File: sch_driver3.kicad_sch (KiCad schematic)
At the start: 17 parts, among them Q3 PSMN4R0-30YLDX, U13 TS5A3159ADCK, U2 ADA4099-2xR, U23 OPA333

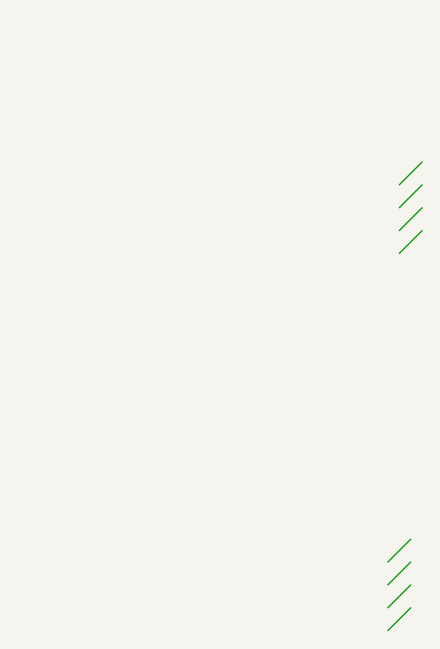
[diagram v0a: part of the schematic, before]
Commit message: Finished schematic refactor to six A-sheets. Updated PCB.
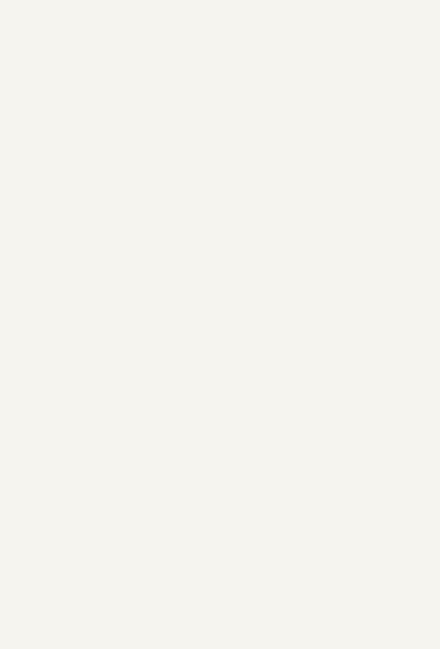
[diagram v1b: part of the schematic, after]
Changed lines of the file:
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@@
 	(title_block
 		(title "PBM Driver 4 V2")
-		(date "23-DEC-2025")
+		(date "24-DEC-2025")
 		(rev "A")
 		(comment 1 "Part Number: PCB104 Rev A")
@@
 		(color 0 0 0 0)
 	)
-	(bus_entry
-		(at 389.89 226.06)
-		(size -2.54 2.54)
-		(stroke
-			(width 0)
-			(type default)
-		)
-	)
-	(bus_entry
-		(at 389.89 223.52)
-		(size -2.54 2.54)
-		(stroke
-			(width 0)
-			(type default)
-		)
-	)
-	(bus_entry
-		(at 391.16 181.61)
-		(size -2.54 2.54)
-		(stroke
-			(width 0)
-			(type default)
-		)
-	)
-	(bus_entry
-		(at 391.16 179.07)
-		(size -2.54 2.54)
-		(stroke
-			(width 0)
-			(type default)
-		)
-	)
-	(bus_entry
-		(at 389.89 220.98)
-		(size -2.54 2.54)
-		(stroke
-			(width 0)
-			(type default)
-		)
-	)
-	(bus_entry
-		(at 391.16 184.15)
-		(size -2.54 2.54)
-		(stroke
-			(width 0)
-			(type default)
-		)
-	)
-	(bus_entry
-		(at 391.16 176.53)
-		(size -2.54 2.54)
-		(stroke
-			(width 0)
-			(type default)
-		)
-	)
-	(bus_entry
-		(at 389.89 218.44)
-		(size -2.54 2.54)
-		(stroke
-			(width 0)
-			(type default)
-		)
-	)
 	(wire

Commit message: Routing WIP. Prep to look at SOT-23 op amps for U1 and U2. Added convenience link to Git Bash.
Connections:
- net OUT: now reaches C33.2, R13.1, U2.1
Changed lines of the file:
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@@
+		)
+	)
+	(label "OUT"
+		(at 110.49 53.34 0)
+		(effects
+			(font
+				(size 1.27 1.27)
+			)
+			(justify left bottom)
 		)
 	)

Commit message: Routing WIP with SOT-23 op amps
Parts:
- added C53: 100pF, $Local:C_0603_1608Metric, symbol $Local:C
- added U5: ADA4099-2xR, Package_TO_SOT_SMD:TSOT-23-6, symbol Amplifier_Operational:ADA4099-1xUJ
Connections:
- net +12V: now also U5.6 (V+)
- net DAC: now also C53.1
- net FB: now also U5.4 (-)
- net GND: now also C53.2, U5.2 (V-), U5.5 (~{SHDN})
- net OUT: now also U5.1
- net REF: now also U5.3 (+)

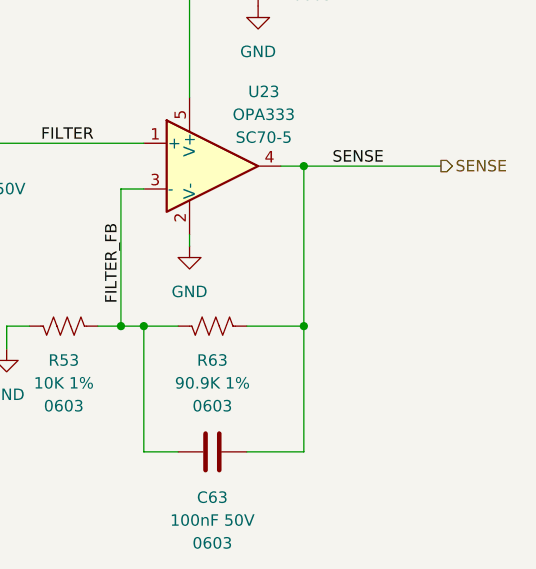
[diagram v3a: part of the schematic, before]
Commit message: Added pull-downs to output of Sense filter op amps
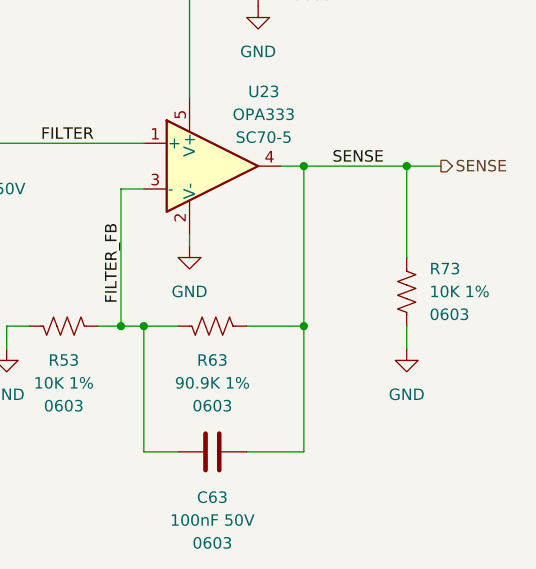
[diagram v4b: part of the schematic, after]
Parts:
- added R73: 10K 1%, $Local:R_0603_1608Metric, symbol $Local:R_0603_10K
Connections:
- net GND: now also R73.2
- net SENSE: now also R73.1
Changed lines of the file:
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@@
 		(color 0 0 0 0)
 	)
+	(junction
+		(at 237.49 71.12)
+		(diameter 0)
+		(color 0 0 0 0)
+	)
 	(wire
 		(pts
@@
 	(wire
 		(pts
+			(xy 237.49 71.12) (xy 241.3 71.12)
+		)
+		(stroke
+			(width 0)
+			(type default)
+		)
+	)
+	(wire
+		(pts
 			(xy 208.28 88.9) (xy 212.09 88.9)
 		)
@@
 	(wire
 		(pts
+			(xy 237.49 71.12) (xy 237.49 81.28)
+		)
+		(stroke
+			(width 0)
+			(type default)
+		)
+	)
+	(wire
+		(pts
 			(xy 54.61 55.88) (xy 54.61 53.34)
 		)
@@
 	(wire
 		(pts
-			(xy 226.06 71.12) (xy 241.3 71.12)
+			(xy 226.06 71.12) (xy 237.49 71.12)
 		)
 		(stroke
@@
 		(pts
 			(xy 147.32 58.42) (xy 147.32 60.96)
+		)
+		(stroke
+			(width 0)
+			(type default)
+		)
+	)
+	(wire
+		(pts
+			(xy 237.49 88.9) (xy 237.49 91.44)
 		)
 		(stroke
@@
 					(unit 1)
 				)
+			)
+		)
+	)
+	(symbol
+		(lib_id "$Local:R_0603_10K")
+		(at 237.49 85.09 0)
+		(unit 1)
+		(exclude_from_sim no)
+		(in_bom yes)
+		(on_board yes)
+		(dnp no)
+		(fields_autoplaced yes)
+		(property "Reference" "R73"
+			(at 240.03 82.5499 0)
+			(effects
+				(font
+					(size 1.27 1.27)
+				)
+				(justify left)
+			)
+		)
+		(property "Value" "10K 1%"
+			(at 240.03 85.0899 0)
+			(effects
+				(font
+					(size 1.27 1.27)
+				)
+				(justify left)
+			)
+		)
+		(property "Footprint" "$Local:R_0603_1608Metric"
+			(at 238.506 85.344 90)
+			(effects
+				(font
+					(size 1.27 1.27)
+				)
+				(hide yes)
+			)
+		)
+		(property "Datasheet" "~"
+			(at 237.49 85.09 0)
+			(effects
+				(font
+					(size 1.27 1.27)
+				)
+				(hide yes)
+			)
+		)
+		(property "Description" "RES SMD 10K OHM 1% 1/10W 0603"
+			(at 237.49 85.09 0)
+			(effects
+				(font
+					(size 1.27 1.27)
+				)
+				(hide yes)
+			)
+		)
+		(property "Size" "0603"
+			(at 240.03 87.6299 0)
+			(effects
+				(font
+					(size 1.27 1.27)
+				)
+				(justify left)
+			)
+		)
+		(property "PN" ""
+			(at 237.49 85.09 0)
+			(effects
+				(font
+					(size 1.27 1.27)
+				)
+				(hide yes)
+			)
+		)
+		(pin "1"
+		)
+		(pin "2"
+		)
+		(instances
+			(project "pbm_driver4_v2"
+				(path "/04797749-7aaf-42f7-a5f4-0b9aeb0ad7be/8ef61302-d9b8-4eae-8136-04cfb82addb3"
+					(reference "R73")
+					(unit 1)
+				)
+			)
+		)
+	)
+	(symbol
+		(lib_id "$Local:GND")
+		(at 237.49 91.44 0)
+		(unit 1)
+		(exclude_from_sim no)
+		(in_bom yes)
+		(on_board yes)
+		(dnp no)
+		(fields_autoplaced yes)
+		(property "Reference" "#PWR036"
+			(at 237.49 97.79 0)
+			(effects
+				(font
+					(size 1.27 1.27)
+				)
+				(hide yes)
+			)
+		)
+		(property "Value" "GND"
+			(at 237.49 96.52 0)
+			(effects
+				(font
+					(size 1.27 1.27)
+				)
+			)
+		)
+		(property "Footprint" ""
+			(at 237.49 91.44 0)
+			(effects
+				(font
+					(size 1.27 1.27)
+				)
+				(hide yes)
+			)
+		)
+		(property "Datasheet" ""
+			(at 237.49 91.44 0)
+			(effects
+				(font
+					(size 1.27 1.27)
+				)
+				(hide yes)
+			)
+		)
+		(property "Description" "Power symbol creates a global label with name \"GND\" , ground"
+			(at 237.49 91.44 0)
+			(effects
+				(font
+					(size 1.27 1.27)
+				)
+				(hide yes)
+			)
+		)
+		(pin "1"
+		)
+		(instances
+			(project "pbm_driver4_v2"
+				(path "/04797749-7aaf-42f7-a5f4-0b9aeb0ad7be/8ef61302-d9b8-4eae-8136-04cfb82addb3"
+					(reference "#PWR036")
+					(unit 1)
+				)

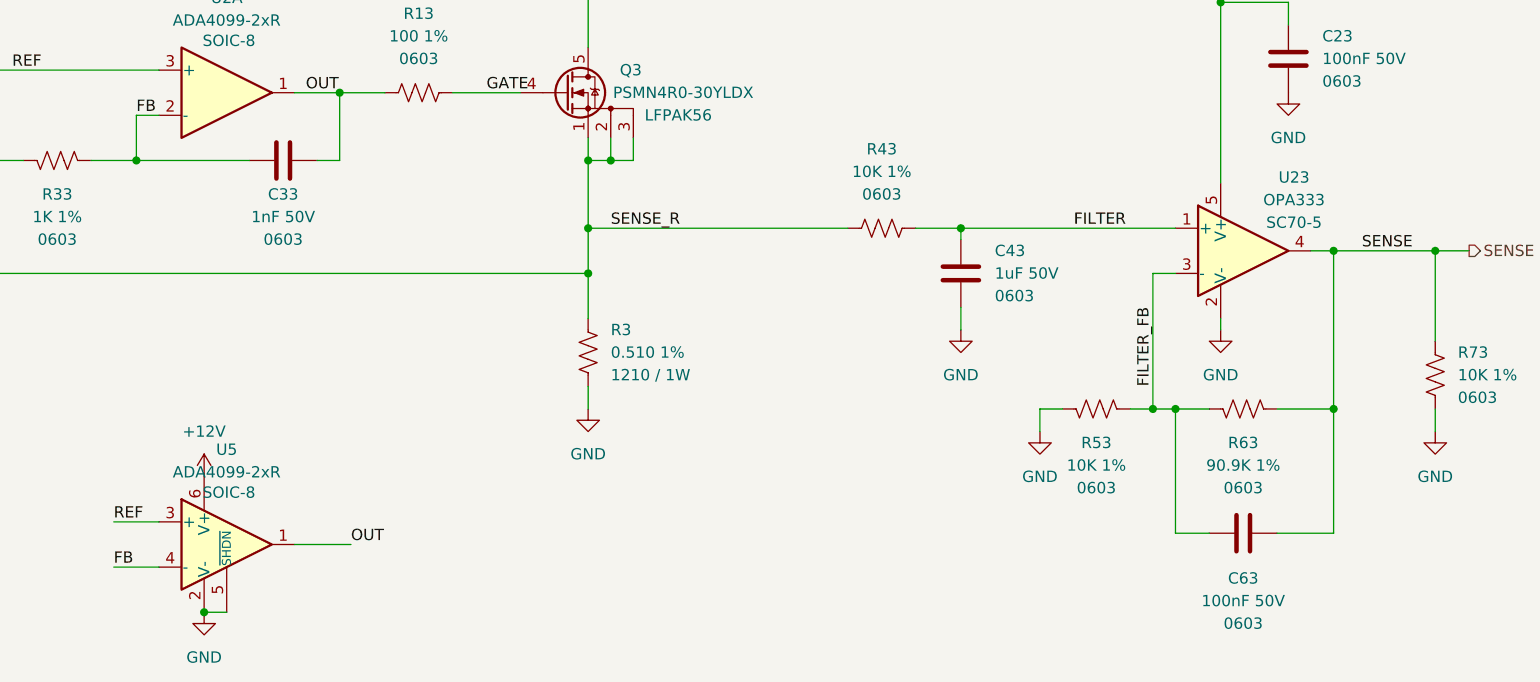
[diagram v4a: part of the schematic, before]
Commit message: Change schematic sense buffer vrom OPA333 in SC70 to OPA365 in SOT-23
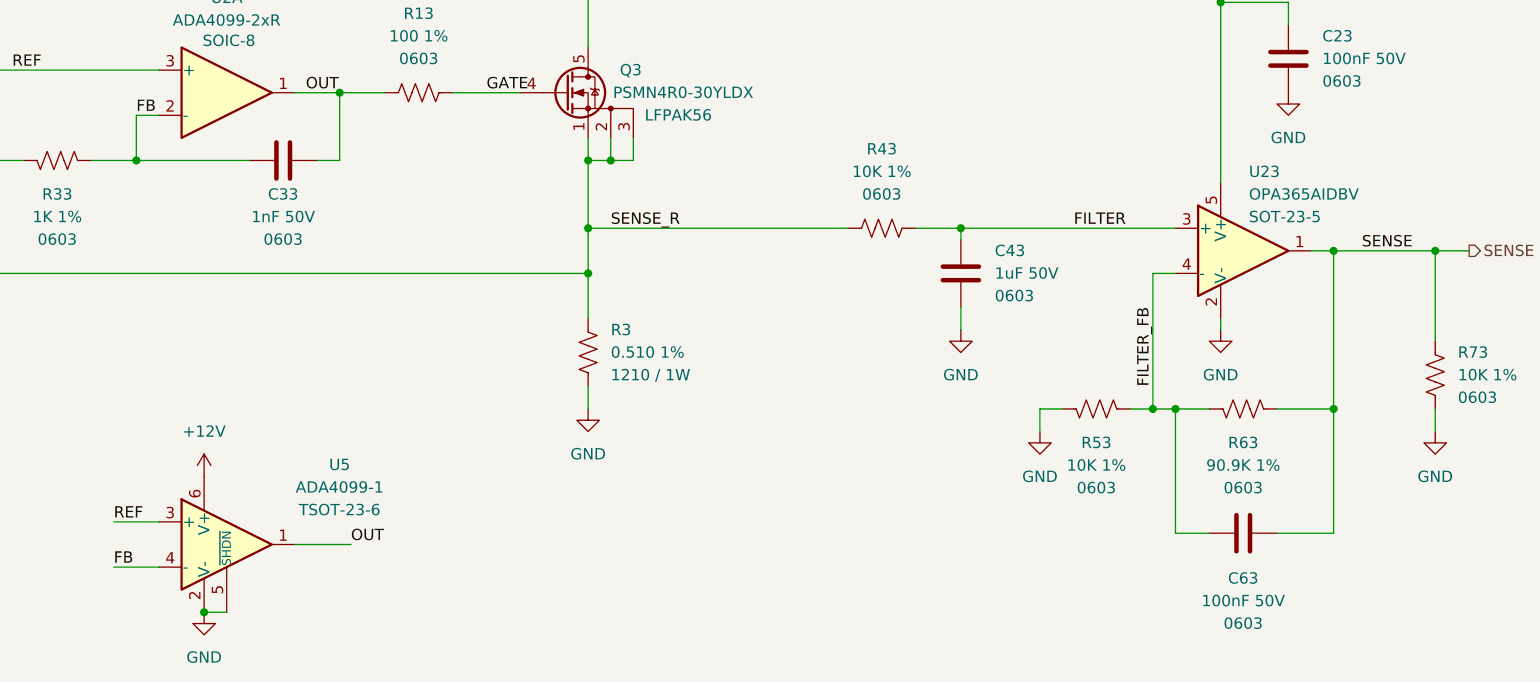
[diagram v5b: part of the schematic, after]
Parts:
- removed U23: OPA333, Package_TO_SOT_SMD:SOT-353_SC-70-5, symbol $Local:OPA333
- removed U5: ADA4099-2xR, Package_TO_SOT_SMD:TSOT-23-6, symbol Amplifier_Operational:ADA4099-1xUJ
- added U23: OPA365AIDBV, $Local:SOT-23-5, symbol $Local:OPA365AIDBV
- added U5: ADA4099-1, $Local:TSOT-23-6, symbol $Local:ADA4099-1
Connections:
- net +12V: now also U5.6 (V+)
- net +3.3V: now also U23.5 (V+)
- net FB: now also U5.4 (-)
- net FILTER: now also U23.3 (+)
- net FILTER_FB: now also U23.4 (-)
- net GND: now also U23.2 (V-), U5.2 (V-), U5.5 (~{SHDN})
- net OUT: now also U5.1
- net REF: now also U5.3 (+)
- net SENSE: now also U23.1
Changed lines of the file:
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@@
 	)
 	(junction
-		(at 33.02 48.26)
+		(at 99.06 111.76)
 		(diameter 0)
 		(color 0 0 0 0)
 	)
 	(junction
-		(at 95.25 147.32)
+		(at 33.02 48.26)
 		(diameter 0)
 		(color 0 0 0 0)
 	)
 	(junction
-		(at 226.06 71.12)
+		(at 95.25 147.32)
 		(diameter 0)
 		(color 0 0 0 0)
 	)
 	(junction
-		(at 99.06 111.76)
+		(at 226.06 71.12)
 		(diameter 0)
 		(color 0 0 0 0)
@@
 	)
 	(symbol
+		(lib_id "$Local:OPA365AIDBV")
+		(at 215.9 71.12 0)
+		(unit 1)
+		(exclude_from_sim no)
+		(in_bom yes)
+		(on_board yes)
+		(dnp no)
+		(property "Reference" "U23"
+			(at 216.535 62.23 0)
+			(effects
+				(font
+					(size 1.27 1.27)
+				)
+				(justify left)
+			)
+		)
+		(property "Value" "OPA365AIDBV"
+			(at 216.535 64.77 0)
+			(effects
+				(font
+					(size 1.27 1.27)
+				)
+				(justify left)
+			)
+		)
+		(property "Footprint" "$Local:SOT-23-5"
+			(at 213.36 76.2 0)
+			(effects
+				(font
+					(size 1.27 1.27)
+				)
+				(justify left)
+				(hide yes)
+			)
+		)
+		(property "Datasheet" "https://www.ti.com/lit/ds/symlink/opa365.pdf"
+			(at 215.9 66.04 0)
+			(effects
+				(font
+					(size 1.27 1.27)
+				)
+				(hide yes)
+			)
+		)
+		(property "Description" "50-MHz, Zero-Crossover, Low-Distortion, High CMRR, RRI/O, Single-Supply, SOT-23-5"
+			(at 215.9 71.12 0)
+			(effects
+				(font
+					(size 1.27 1.27)
+				)
+				(hide yes)
+			)
+		)
+		(property "Package" "SOT-23-5"
+			(at 216.535 67.31 0)
+			(effects
+				(font
+					(size 1.27 1.27)
+				)
+				(justify left)
+			)
+		)
+		(property "Digikey" "296-26283-1-ND"
+			(at 215.9 71.12 0)
+			(effects
+				(font
+					(size 1.27 1.27)
+				)
+				(hide yes)
+			)
+		)
+		(pin "1"
+		)
+		(pin "5"
+		)
+		(pin "2"
+		)
+		(pin "4"
+		)
+		(pin "3"
+		)
+		(instances
+			(project "pbm_driver4_v2"
+				(path "/04797749-7aaf-42f7-a5f4-0b9aeb0ad7be/8ef61302-d9b8-4eae-8136-04cfb82addb3"
+					(reference "U23")
+					(unit 1)
+				)
+			)
+		)
+	)
+	(symbol
 		(lib_id "$Local:GND")
 		(at 237.49 91.44 0)
@@
 	)
 	(symbol
-		(lib_id "$Local:OPA333")
-		(at 215.9 71.12 0)
-		(unit 1)
-		(exclude_from_sim no)
-		(in_bom yes)
-		(on_board yes)
-		(dnp no)
-		(property "Reference" "U23"
-			(at 221.615 62.865 0)
-			(effects
-				(font
-					(size 1.27 1.27)
-				)
-			)
-		)
-		(property "Value" "OPA333"
-			(at 221.615 65.405 0)
-			(effects
-				(font
-					(size 1.27 1.27)
-				)
-			)
-		)
-		(property "Footprint" "Package_TO_SOT_SMD:SOT-353_SC-70-5"
-			(at 215.9 71.12 0)
-			(effects
-				(font
-					(size 1.27 1.27)
-				)
-				(justify left)
-				(hide yes)
-			)
-		)
-		(property "Datasheet" ""
-			(at 215.9 71.12 0)
-			(effects
-				(font
-					(size 1.27 1.27)
-				)
-				(hide yes)
-			)
-		)
-		(property "Description" "Low-Voltage Rail-to-Rail Output Operational Amplifier, SC-70-5"
-			(at 215.9 71.12 0)
-			(effects
-				(font
-					(size 1.27 1.27)
-				)
-				(hide yes)
-			)
-		)
-		(property "Package" "SC70-5"
-			(at 221.615 67.945 0)
-			(effects
-				(font
-					(size 1.27 1.27)
-				)
-			)
-		)
-		(pin "1"
-		)
-		(pin "5"
-		)
-		(pin "2"
-		)
-		(pin "3"
-		)
-		(pin "4"
-		)
-		(instances
-			(project ""
-				(path "/04797749-7aaf-42f7-a5f4-0b9aeb0ad7be/69524e69-370d-45a1-972c-d2766add5424"
-					(reference "U21")
-					(unit 1)
-				)
-				(path "/04797749-7aaf-42f7-a5f4-0b9aeb0ad7be/8ef61302-d9b8-4eae-8136-04cfb82addb3"
-					(reference "U23")
-					(unit 1)
-				)
-			)
-		)
-	)
-	(symbol
 		(lib_id "$Local:R_0603_10K")
 		(at 41.91 64.77 0)
@@
 	)
 	(symbol
+		(lib_id "$Local:ADA4099-1")
+		(at 101.6 104.14 0)
+		(unit 1)
+		(exclude_from_sim no)
+		(in_bom yes)
+		(on_board yes)
+		(dnp no)
+		(fields_autoplaced yes)
+		(property "Reference" "U5"
+			(at 114.3 95.1798 0)
+			(effects
+				(font
+					(size 1.27 1.27)
+				)
+			)
+		)
+		(property "Value" "ADA4099-1"
+			(at 114.3 97.7198 0)
+			(effects
+				(font
+					(size 1.27 1.27)
+				)
+			)
+		)
+		(property "Footprint" "$Local:TSOT-23-6"
+			(at 101.6 110.49 0)
+			(effects
+				(font
+					(size 1.27 1.27)
+				)
+				(hide yes)
+			)
+		)
+		(property "Datasheet" "https://www.analog.com/media/en/technical-documentation/data-sheets/ada4099-1_ada4099-2.pdf"
+			(at 101.6 113.03 0)
+			(effects
+				(font
+					(size 1.27 1.27)
+				)
+				(justify left)
+				(hide yes)
+			)
+		)
+		(property "Description" "3.15..50V supply, 8MHz GBW, Rail-to-Rail input/output, over-the-top opamp with shutdown, TSOT-6"
+			(at 101.6 104.14 0)
+			(effects
+				(font
+					(size 1.27 1.27)
+				)
+				(hide yes)
+			)
+		)
+		(property "Package" "TSOT-23-6"
+			(at 114.3 100.2598 0)
+			(effects
+				(font
+					(size 1.27 1.27)
+				)
+			)
+		)
+		(property "Digikey" "505-ADA4099-1BUJZ-RL7CT-ND"
+			(at 101.6 104.14 0)
+			(effects
+				(font
+					(size 1.27 1.27)
+				)
+				(hide yes)
+			)
+		)
+		(pin "3"
+		)
+		(pin "6"
+		)
+		(pin "1"
+		)
+		(pin "5"
+		)
+		(pin "4"
+		)
+		(pin "2"
+		)
+		(instances
+			(project "pbm_driver4_v2"
+				(path "/04797749-7aaf-42f7-a5f4-0b9aeb0ad7be/8ef61302-d9b8-4eae-8136-04cfb82addb3"
+					(reference "U5")
+					(unit 1)
+				)
+			)
+		)
+	)
+	(symbol
 		(lib_id "$Local:GND")
 		(at 33.02 71.12 0)
@@
 					(unit 1)
 				)
-			)
-		)
-	)
-	(symbol
-		(lib_id "Amplifier_Operational:ADA4099-1xUJ")
-		(at 101.6 104.14 0)
-		(unit 1)
-		(exclude_from_sim no)
-		(in_bom yes)
-		(on_board yes)
-		(dnp no)
-		(property "Reference" "U5"
-			(at 101.6 93.472 0)
-			(effects
-				(font
-					(size 1.27 1.27)
-				)
-			)
-		)
-		(property "Value" "ADA4099-2xR"
-			(at 101.6 96.012 0)
-			(effects
-				(font
-					(size 1.27 1.27)
-				)
-			)
-		)
-		(property "Footprint" "Package_TO_SOT_SMD:TSOT-23-6"
-			(at 101.6 110.49 0)
-			(effects
-				(font
-					(size 1.27 1.27)
-				)
-				(hide yes)
-			)
-		)
-		(property "Datasheet" "https://www.analog.com/media/en/technical-documentation/data-sheets/ada4099-1_ada4099-2.pdf"
-			(at 101.6 113.03 0)
-			(effects
-				(font
-					(size 1.27 1.27)
-				)
-				(justify left)
-				(hide yes)
-			)
-		)
-		(property "Description" "3.15..50V supply, 8MHz GBW, Rail-to-Rail input/output, over-the-top opamp with shutdown, TSOT-6"
-			(at 101.6 104.14 0)
-			(effects
-				(font
-					(size 1.27 1.27)
-				)
-				(hide yes)
-			)
-		)
-		(property "Digikey" "505-ADA4099-2BRZ-ND"
-			(at 101.6 104.14 0)
-			(effects
-				(font
-					(size 1.27 1.27)
-				)
-				(hide yes)
-			)
-		)
-		(property "PN" "505-ADA4099-2BRZ-ND"
-			(at 101.6 104.14 0)
-			(effects
-				(font
-					(size 1.27 1.27)
-				)
-				(hide yes)
-			)
-		)
-		(property "Package" "SOIC-8"
-			(at 101.854 98.298 0)
-			(effects
-				(font
-					(size 1.27 1.27)
-				)
-			)
-		)
-		(pin "1"
-		)
-		(pin "3"
-		)
-		(pin "2"
-		)
-		(pin "6"
-		)
-		(pin "5"
-		)
-		(pin "4"
-		)
-		(instances
-			(project "pbm_driver4_v2"
-				(path "/04797749-7aaf-42f7-a5f4-0b9aeb0ad7be/8ef61302-d9b8-4eae-8136-04cfb82addb3"
-					(reference "U5")
-					(unit 1)
-				)
